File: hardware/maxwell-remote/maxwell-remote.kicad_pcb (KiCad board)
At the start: 2 copper layers, 71.1 x 38.1 mm, 43 parts, among them J1 INPUT, J3 Left, J4 Right, J5 Programmer, Q2 NDS332P, Q3 NDS332P, Q4 NDS332P, U1 STM32F103C8Tx, U3 MIC5209-ADJ, U5 SN65HVD235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

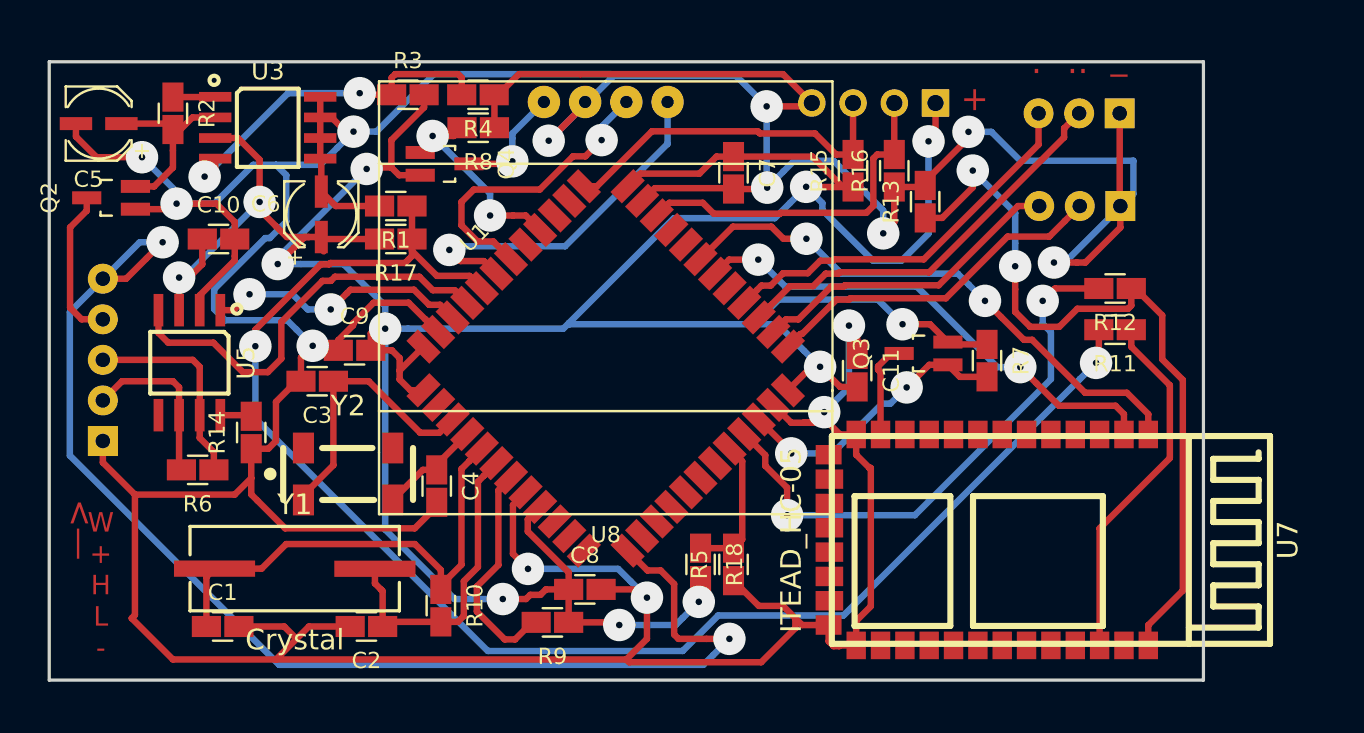
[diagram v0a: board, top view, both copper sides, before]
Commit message: Updating maxwell-remote to v2.0; adds a variety of fixes including:
Layout:

* Use of incorrect footprint for NDS332 (should be SSOT-3 rathe
  than SOT-23)
* Inverted default powered states for screen and bluetooth module.
* Fixed 32kHz crystal footprint.
* Swapped surface-mount capacitors for through-hole for durability.
  I've torn the surface-mount ones off the board at least twice now;
  they are not likely to survive long in a high-vibration environment.
* General layout improvements.

Functional:

* Linked both UART2 and UART1 to Bluetooth module.  Only UART1 can be
  used for programming, but UART1 is _usually_ used for SerialUSB and
  thus should be avoided given that the USB hardware shares memory with
  the CAN hardware.
* Added a RX/TX JST connector.  This is partially to improve my ability
  to solder to the fcu layer (by adding an additional plastic support to
  the underside of the board), but also because it does make it easier
  to troubleshoot.
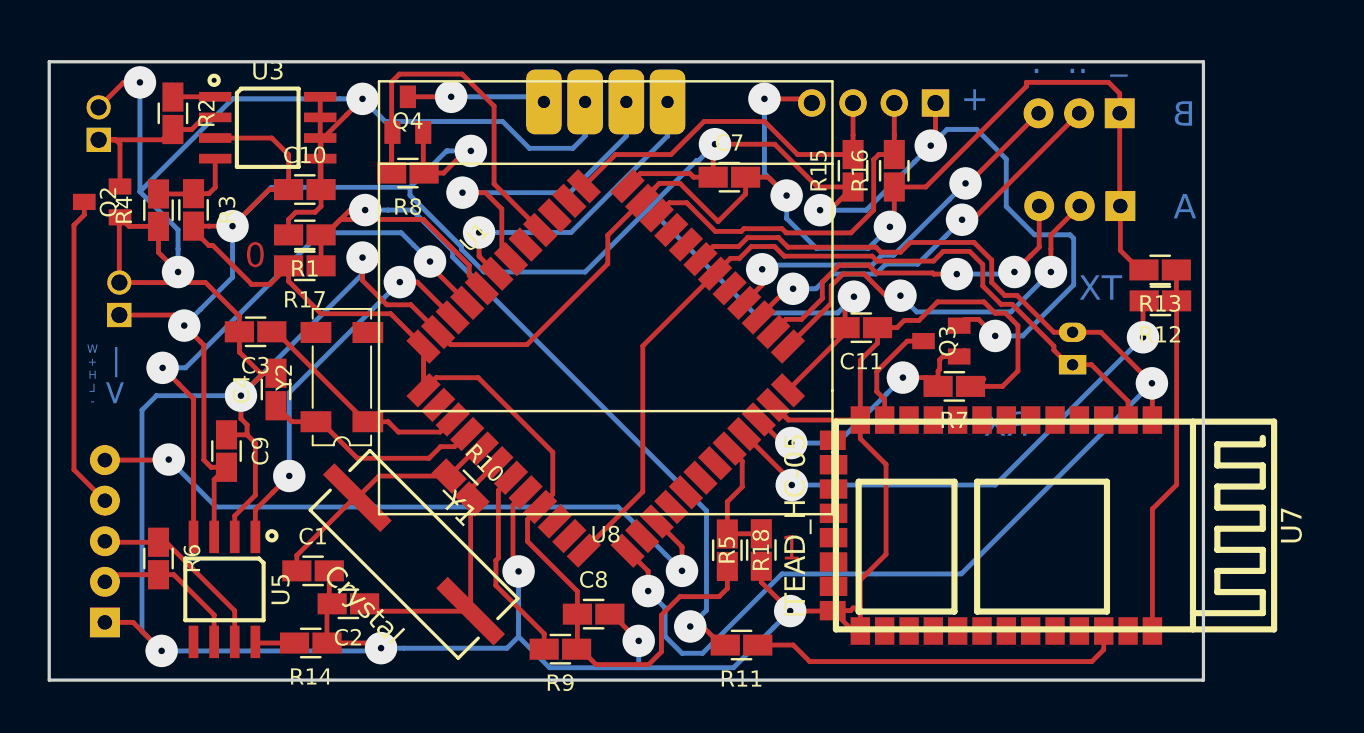
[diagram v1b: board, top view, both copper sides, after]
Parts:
- added J2: UART, KiCad/Connectors_JST.pretty:JST_PH_B2B-PH-K_02x2.00mm_Straight, B.Cu at (160.8, 74.5)
- C5, C6: footprint celeritous/KiCad.pretty:CAPACITOR_ELECTROLYTIC_4.3MM -> usagi1975/kicad_mod.pretty:Capacitor_Electrolytic_D5.0xP2.0; moved to B.Cu
- Q2, Q3, Q4: footprint cuzdaori/KiCad.pretty:SOT23 -> cvra/kicad-lib/footprints/_std.pretty:SSOT-3
- Y2: footprint hairymnstr/Nathan_SMT_Other.pretty:MC306 -> KiCad/Crystals.pretty:Crystal_SMD_SeikoEpson_MC306-4pin_8.0x3.2mm
- moved R11 30.1 mm to (140.4, 91.8)
- moved R4 20.9 mm to (104.5, 65.0), turned to 90 degrees
- moved R13 15.1 mm to (166.2, 68.7), turned to 180 degrees
- moved R3 15.0 mm to (106.7, 65.0), turned to 270 degrees
- moved U5 14.1 mm to (108.6, 88.4)
- moved C6 13.5 mm to (102.1, 70.5), turned to 180 degrees
- moved R14 13.5 mm to (113.9, 91.7), turned to 180 degrees
- moved C4 11.6 mm to (111.8, 76.1), turned to 90 degrees
- moved J1 11.2 mm to (101.2, 90.4)
- moved C9 10.0 mm to (108.7, 79.9), turned to 270 degrees
- moved Y1 7.41 mm to (120.3, 86.2), turned to 315 degrees
- moved R10 7.38 mm to (123.1, 82.1), turned to 315 degrees
- moved C1 6.54 mm to (114.0, 87.2)
- moved C10 6.13 mm to (113.5, 63.8)
- moved Y2 5.98 mm to (115.8, 75.3), turned to 90 degrees
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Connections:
- R7 pad 1: +3V3 -> GND
- R8 pad 1: GND -> +3V3
- U1 pad 12: Net-(U1-Pad12) -> TX
- U1 pad 13: WAKE -> RX
- U1 pad 15: Net-(U1-Pad15) -> WAKE
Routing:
- net RX: track 34.5 -> 79.2 mm
- net BOOT0: track 93.3 -> 56.5 mm
- net WAKE: track 78.0 -> 42.1 mm
- net Net-(R12-Pad1): track 48.0 -> 22.9 mm, vias 2 -> 0
- net TX: track 30.8 -> 53.1 mm, vias 2 -> 0
- net Net-(R3-Pad1): track 21.8 -> 5.43 mm, vias 2 -> 0
- net GND: track 359.9 -> 344.4 mm, vias 14 -> 13
- net Net-(C1-Pad1): track 29.9 -> 15.1 mm
- net +3V3: track 215.8 -> 227.2 mm, vias 12 -> 8
- net ENABLE_SCREEN: track 13.2 -> 24.3 mm, vias 2 -> 0
- net +BATT: track 9.51 -> 19.5 mm
- net CAN_RX: track 25.9 -> 35.4 mm, vias 0 -> 2
- net Net-(C4-Pad1): track 6.47 -> 13.7 mm
- net CAN_TX: track 16.3 -> 23.5 mm
- net ~LEFT_A: track 21.6 -> 25.5 mm, vias 0 -> 2
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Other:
- net class Default: clearance 0.24 -> 0.25; trace_width 0.4 -> 0.3
- rule trace_clearance: 0.24 -> 0.25
- board text added: "0"
- board text added: "1"
- board text added: "A"
- board text added: "B"
- board text added: "RX"
- board text added: "TX"

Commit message: Updating boardfile to include a little logo, and much bigger pads for everything that'll be exposed to physical strain.
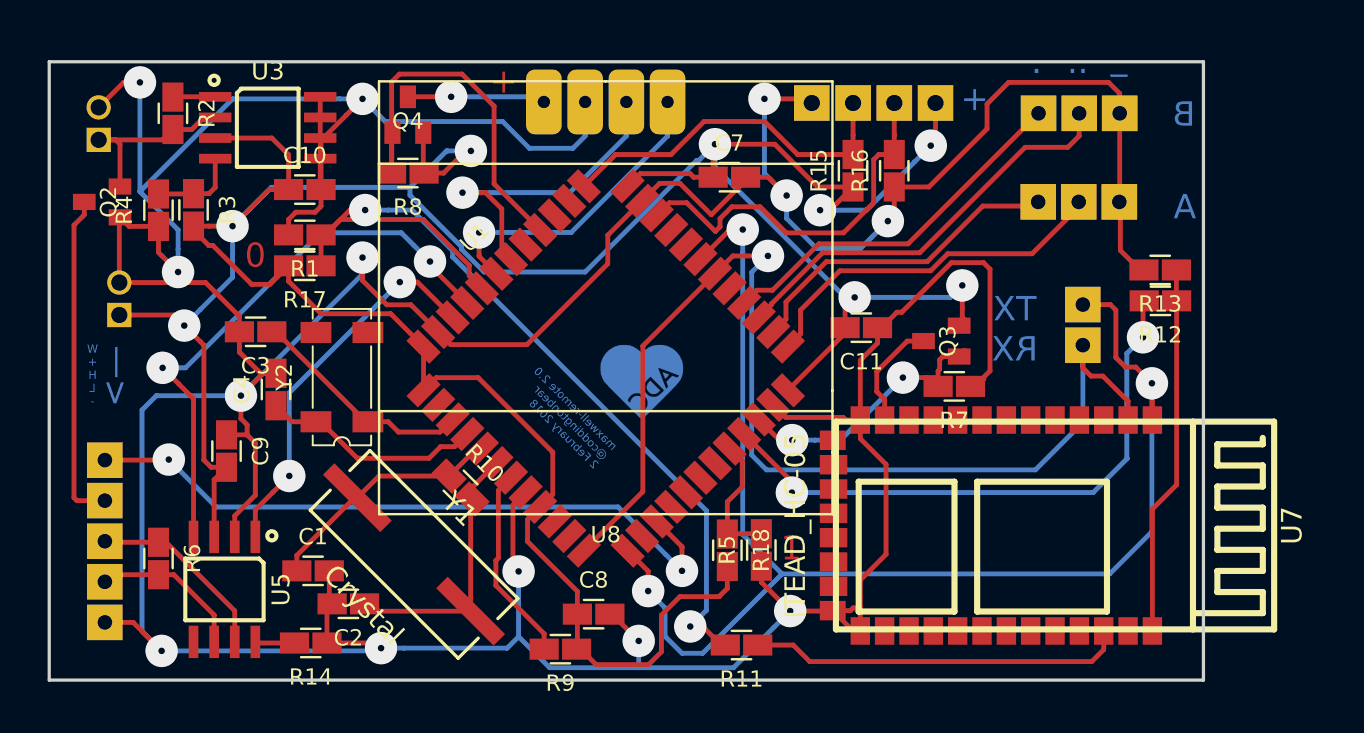
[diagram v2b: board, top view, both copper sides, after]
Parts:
- added G***: LOGO, coddingtonbear:coddingtonbear_logo.B.Cu.5mm, F.Cu at (134.3, 75.6)
- J1: footprint KiCad/Connectors_JST.pretty:JST_EH_B05B-EH-A_05x2.50mm_Straight -> coddingtonbear/coddingtonbear.pretty:JST_EH_B05B-EH-A_05x2.50mm_Straight_LargePads
- J2: footprint KiCad/Connectors_JST.pretty:JST_PH_B2B-PH-K_02x2.00mm_Straight -> coddingtonbear/coddingtonbear.pretty:JST_EH_B02B-EH-A_02x2.50mm_Straight_LargePads
- J3, J4: footprint KiCad/Connectors_JST.pretty:JST_EH_B03B-EH-A_03x2.50mm_Straight -> coddingtonbear/coddingtonbear.pretty:JST_EH_B03B-EH-A_03x2.50mm_Straight_LargePads
- J5: footprint KiCad/Pin_Headers.pretty:Pin_Header_Straight_1x04_Pitch2.54mm -> coddingtonbear/coddingtonbear.pretty:Pin_Header_Straight_1x04_Pitch2.54mm_LargePads
- moved J2 1.36 mm to (161.5, 73.3)
- moved J3 0.26 mm to (163.7, 64.5)
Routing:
- net +3V3: track 227.2 -> 208.9 mm
- net TX: track 53.1 -> 69.8 mm, vias 0 -> 1
- net RX: track 79.2 -> 84.8 mm, vias 2 -> 3
- net BT_KEY: track 32.0 -> 36.5 mm
- net ~LEFT_A: track 25.5 -> 22.4 mm, vias 2 -> 0
- net ~LEFT_B: track 22.1 -> 20.2 mm, vias 2 -> 0
- net SWDIO: track 22.9 -> 24.0 mm
- net +BATT: track 19.5 -> 20.5 mm
- net ~RIGHT_A: track 25.0 -> 25.8 mm, vias 2 -> 0
- net ~RIGHT_B: track 23.5 -> 23.0 mm, vias 2 -> 0
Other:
- net class Default: clearance 0.25 -> 0.195
- rule trace_clearance: 0.25 -> 0.195
- board text added: "maxwell-remote 2.0 @coddingtonbear 2 February 2018"

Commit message: Updating PCB to include a few more Cu text indicators; minor layout improvements.  Down to just 37 vias.
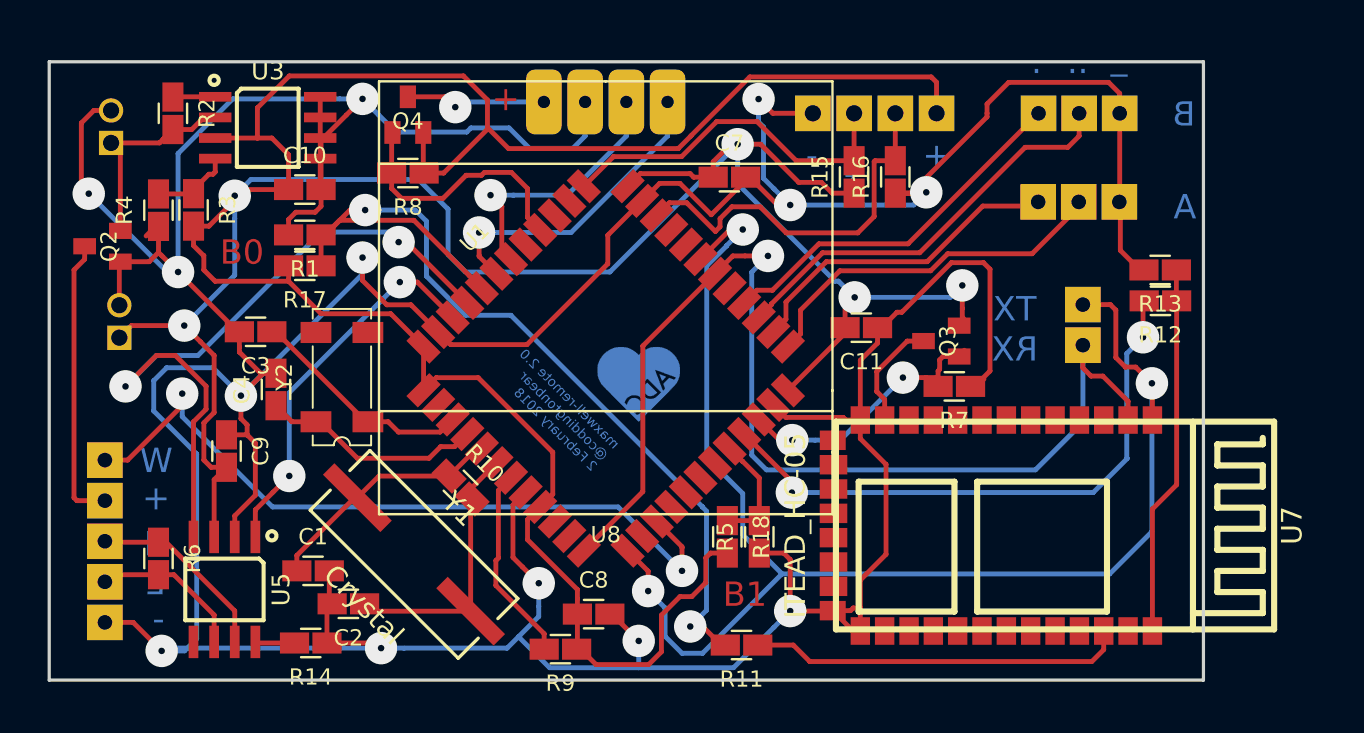
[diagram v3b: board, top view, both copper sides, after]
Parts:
- moved Q2 2.73 mm to (100.0, 67.2)
- moved C6 1.40 mm to (102.1, 71.9)
- moved R18 0.83 mm to (139.6, 85.2)
- moved R5 0.82 mm to (141.5, 85.2)
- moved C5 0.79 mm to (101.6, 59.9)
- moved J5 0.64 mm to (152.5, 59.1)
- moved R15 0.39 mm to (147.4, 63.0)
- moved R16 0.39 mm to (149.9, 63.0)
- moved G*** 0.23 mm to (134.1, 75.8)
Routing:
- net +3V3: track 208.9 -> 248.2 mm, vias 8 -> 5
- net ENABLE_SCREEN: track 24.3 -> 16.0 mm
- net CAN_RX: track 35.4 -> 42.9 mm
- net GND: track 344.6 -> 351.2 mm
- net WAKE: track 42.1 -> 46.7 mm
- net SCL: track 19.8 -> 16.4 mm
- net +BATT: track 20.5 -> 17.7 mm
- net RX: track 84.8 -> 86.6 mm
- net Net-(C5-Pad1): track 11.8 -> 13.6 mm
- net BOOT0: track 56.5 -> 57.9 mm
- net BOOT1: track 8.07 -> 7.18 mm
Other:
- board text added: "-"
- board text added: "B0"
- board text added: "B1"
- board text added: "CLK"
- board text added: "H"
- board text added: "IO"
- board text added: "L"
- board text added: "W"
- board text removed: "0"
- board text removed: "1"
- board text removed: "<—"
- board text removed: "W + H L -"

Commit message: 34 Vias
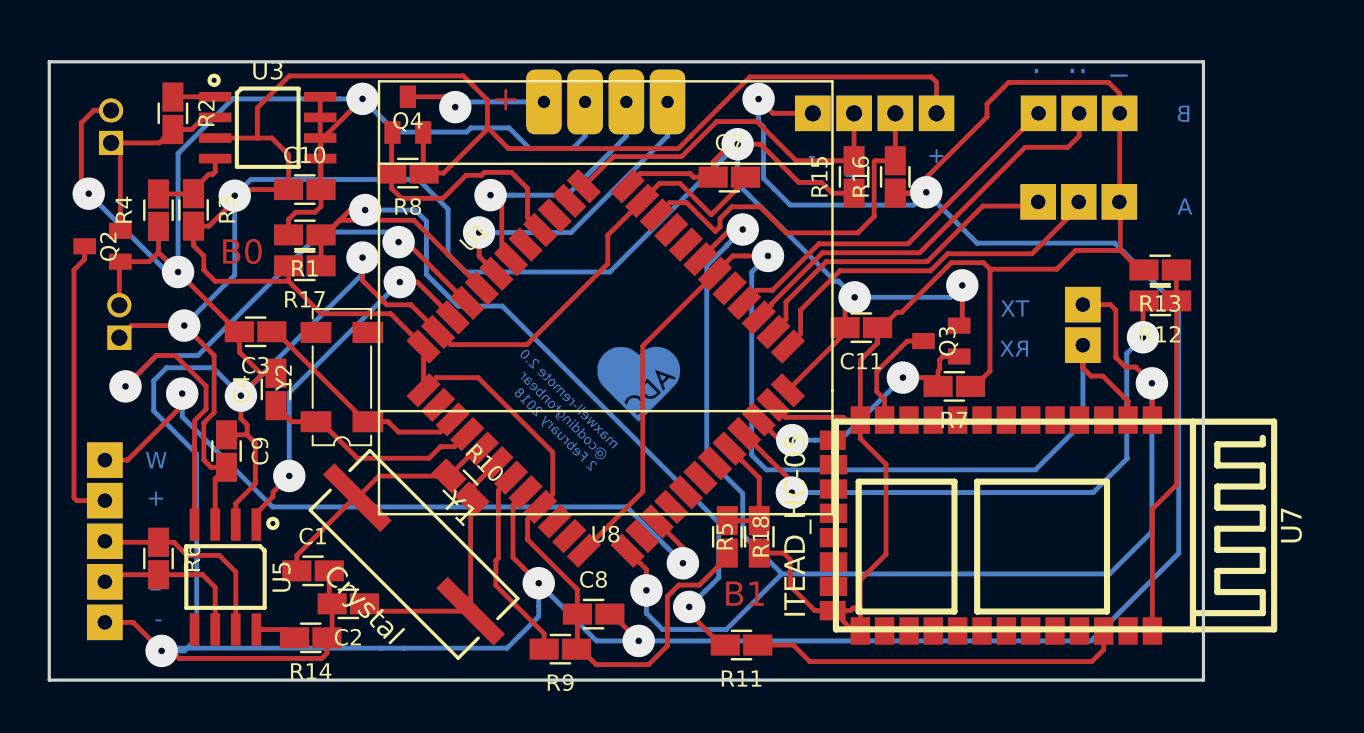
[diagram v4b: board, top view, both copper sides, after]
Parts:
- moved U5 0.76 mm to (108.6, 87.6)
- moved R14 0.32 mm to (113.9, 91.4)
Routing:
- net GND: track 351.2 -> 416.9 mm, vias 13 -> 10
- net RX: track 86.6 -> 85.2 mm
- net CAN+: track 11.7 -> 12.9 mm
- net +3V3: track 248.2 -> 247.1 mm
- net CAN_RX: track 42.9 -> 42.1 mm
- net CAN_TX: track 23.5 -> 22.8 mm
- net WAKE: track 46.7 -> 46.1 mm

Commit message: Better mini unpopulated boot jumper footprint
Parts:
- removed G***: LOGO, coddingtonbear:coddingtonbear_logo.B.Cu.5mm
- removed R17, R18: JMP, coddingtonbear/coddingtonbear.pretty:0805_Milling
- added J6: B0_JMP, coddingtonbear/coddingtonbear.pretty:Pin_Header_Straight_1x02_Pitch1.27mm_JMP, F.Cu at (112.8, 68.5)
- added J7: B1_JMP, coddingtonbear/coddingtonbear.pretty:Pin_Header_Straight_1x02_Pitch1.27mm_JMP, F.Cu at (141.3, 85.4)
- moved R5 1.84 mm to (143.1, 86.1)
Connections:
- net ENABLE_SCREEN renamed ~ENABLE_SCREEN
- net ~DISBABLE_BLUETOOTH renamed DISBABLE_BLUETOOTH
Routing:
- net +3V3: track 247.1 -> 250.4 mm
- net GND: track 416.9 -> 414.7 mm
- net CAN_RX: track 42.1 -> 43.6 mm
- net BOOT1: track 7.18 -> 8.34 mm

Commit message: Maxwell-remote v4; just a ton of changes.
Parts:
- removed Q3: NDS332P, cvra/kicad-lib/footprints/_std.pretty:SSOT-3
- removed R11: 330, coddingtonbear/coddingtonbear.pretty:0805_Milling
- removed U7: ITEAD_HC-05, pelrun/libKiCad/footprint/w_rf_modules.pretty:ITEAD_HC-05
- added C12: 0.1, coddingtonbear/coddingtonbear.pretty:0805_Milling, F.Cu at (165.9, 57.8)
- added J8: SPI2, coddingtonbear:JST_XH_B06B-XH-A_06x2.50mm_Straight_LargePads, B.Cu at (164.2, 83.2)
- added J9: ESP_BM, coddingtonbear/coddingtonbear.pretty:Pin_Header_Straight_1x02_Pitch1.27mm_JMP, F.Cu at (145.4, 74.8)
- added R17: 2.2k, coddingtonbear/coddingtonbear.pretty:0805_Milling, F.Cu at (117.5, 60.1)
- added U2: ESP32-WROOM, OLIMEX/KiCAD/KiCAD_Footprints/OLIMEX_Cases-FP.pretty:ESP-WROOM-32_MODULE, F.Cu at (161.9, 69.2)
- C5: footprint usagi1975/kicad_mod.pretty:Capacitor_Electrolytic_D5.0xP2.0 -> celeritous/KiCad.pretty:CAPACITOR_TANTALUM_B; moved to F.Cu
- C6: footprint usagi1975/kicad_mod.pretty:Capacitor_Electrolytic_D5.0xP2.0 -> celeritous/KiCad.pretty:CAPACITOR_TANTALUM_C; moved to F.Cu
- J1: footprint coddingtonbear/coddingtonbear.pretty:JST_EH_B05B-EH-A_05x2.50mm_Straight_LargePads -> coddingtonbear:JST_XH_B05B-XH-A_05x2.50mm_Straight_LargePads
- J2: footprint coddingtonbear/coddingtonbear.pretty:JST_EH_B02B-EH-A_02x2.50mm_Straight_LargePads -> coddingtonbear:JST_XH_B03B-XH-A_03x2.50mm_Straight_LargePads
- J3, J4: footprint coddingtonbear/coddingtonbear.pretty:JST_EH_B03B-EH-A_03x2.50mm_Straight_LargePads -> coddingtonbear:JST_XH_B03B-XH-A_03x2.50mm_Straight_LargePads
- R12: value 330 -> 10k
- R13: value 10k -> 2.2k
- R7: value 10k -> 330
- U8: footprint coddingtonbear/coddingtonbear.pretty:128x64_OLED_LCD -> coddingtonbear:JST_XH_B04B-XH-A_04x2.50mm_Straight_LargePads; moved to B.Cu
- Y1: footprint brunoeagle/kicad-open-modules:CRYSTAL_SMD -> cpavlina/kicad-pcblib/smd-non-ipc.pretty:Abracon-ABM2
- Y2: value Crystal_GND23_Small -> Crystal_GND23; footprint KiCad/Crystals.pretty:Crystal_SMD_SeikoEpson_MC306-4pin_8.0x3.2mm -> coddingtonbear:SM-CRYSTAL-ABS25_LargePads
- moved R13 43.1 mm to (123.1, 69.8), turned to 315 degrees
- moved R7 36.4 mm to (118.5, 66.0), turned to 0 degrees
- moved J4 31.1 mm to (164.5, 90.2)
- moved J3 27.8 mm to (153.0, 90.2)
- moved J2 19.0 mm to (171.4, 89.5)
- moved R14 13.7 mm to (107.3, 79.4), turned to 90 degrees
- moved R12 13.7 mm to (161.5, 57.8), turned to 0 degrees
- moved U5 13.4 mm to (110.2, 74.3), turned to 90 degrees
- moved C4 11.9 mm to (109.4, 87.8), turned to 180 degrees
- moved Q4 11.7 mm to (129.3, 65.0), turned to 270 degrees
- moved C2 10.7 mm to (105.8, 91.7)
- moved C11 9.62 mm to (146.1, 81.7), turned to 135 degrees
- moved R10 9.19 mm to (115.7, 87.5), turned to 0 degrees
- moved C9 9.14 mm to (116.0, 74.3), turned to 90 degrees
- moved R15 9.01 mm to (138.4, 62.0)
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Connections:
- net Net-(R9-Pad2) renamed NRST
- J2 pad 1: TX -> BT_IN
- J2 pad 2: RX -> BT_OUT
- R12 pad 1: Net-(R12-Pad1) -> DISBABLE_BLUETOOTH_
- R12 pad 2: BT_KEY -> +3V3
- R13 pad 1: Net-(R12-Pad1) -> +3V3
- R13 pad 2: GND -> SCL
- R7 pad 1: GND -> BOOT0
- R7 pad 2: DISBABLE_BLUETOOTH -> Net-(R7-Pad2)
- U1 pad 12: TX -> Net-(U1-Pad12)
- U1 pad 13: RX -> Net-(U1-Pad13)
- U1 pad 14: Net-(U1-Pad14) -> ~RIGHT_A
- U1 pad 15: WAKE -> ~RIGHT_B
- U1 pad 16: Net-(U1-Pad16) -> ~LEFT_B
- U1 pad 17: Net-(U1-Pad17) -> ~LEFT_A
- U1 pad 2: Net-(U1-Pad2) -> WAKE
- U1 pad 21: BT_KEY -> Net-(U1-Pad21)
- U1 pad 22: DISBABLE_BLUETOOTH -> ESP_BOOT_MODE
- U1 pad 25: ~LEFT_A -> Net-(U1-Pad25)
- U1 pad 26: ~LEFT_B -> Net-(J8-Pad5)
- U1 pad 27: ~RIGHT_A -> Net-(J8-Pad4)
- U1 pad 28: ~RIGHT_B -> Net-(J8-Pad3)
- U1 pad 29: Net-(U1-Pad29) -> SPI_CS
- U1 pad 30: TX -> MC_OUT
- U1 pad 31: RX -> MC_IN
- U1 pad 32: Net-(U1-Pad32) -> BT_KEY
- U1 pad 33: Net-(U1-Pad33) -> DISBABLE_BLUETOOTH_
- Y1 pad 1: Net-(C1-Pad1) -> Net-(C2-Pad1)
- Y1 pad 2: Net-(C2-Pad1) -> Net-(C1-Pad1)
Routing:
- net RX: track 85.2 -> 0.00 mm, vias 3 -> 0
- net GND: track 414.7 -> 333.0 mm, vias 10 -> 7
- net +BATT: track 17.7 -> 95.9 mm, vias 0 -> 2
- net TX: track 69.8 -> 0.00 mm, vias 1 -> 0
- net NRST: track 12.2 -> 79.3 mm, vias 0 -> 2
- net BOOT0: track 58.4 -> 13.6 mm, vias 2 -> 0
- net +3V3: track 250.4 -> 207.6 mm, vias 5 -> 9
- net DISBABLE_BLUETOOTH_: track 0.00 -> 40.2 mm
- net Net-(R7-Pad2): track 0.00 -> 39.9 mm, vias 0 -> 2
- net CAN_RX: track 43.6 -> 11.7 mm, vias 2 -> 0
- net SPI_CS: track 0.00 -> 29.8 mm
- net Net-(J8-Pad3): track 0.00 -> 23.5 mm
- net Net-(R11-Pad1): track 23.2 -> 0.00 mm
- net Net-(R12-Pad1): track 22.9 -> 0.00 mm
- net ESP_BOOT_MODE: track 0.00 -> 22.1 mm, vias 0 -> 2
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- added copper zone on F.Cu, net GND
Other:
- board size 71.1 x 38.1 mm -> 77.5 x 38.1 mm
- board text added: "*"
- board text added: "C"
- board text added: "I"
- board text added: "O"
- board text added: "maxwell-remote 3.0 @coddingtonbear 8 April 2018"
- board text removed: "."
- board text removed: ".."
- board text removed: "A"
- board text removed: "B"
- board text removed: "CLK"
- board text removed: "maxwell-remote 2.0 @coddingtonbear 2 February 2018"
